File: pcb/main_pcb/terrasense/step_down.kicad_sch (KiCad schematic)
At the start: 12 parts, among them J12 12V In, U2 Mini560, U4 MPM3632CGQV-P

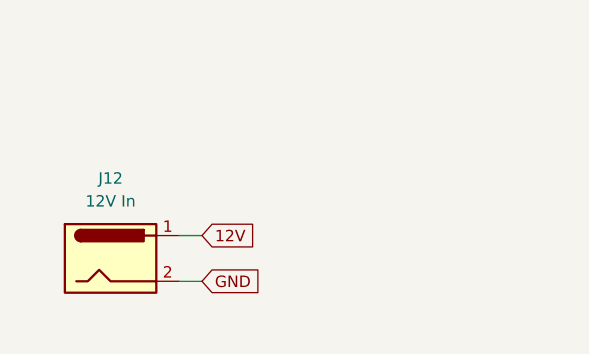
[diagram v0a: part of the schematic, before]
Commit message: update pcb with ordered pcb
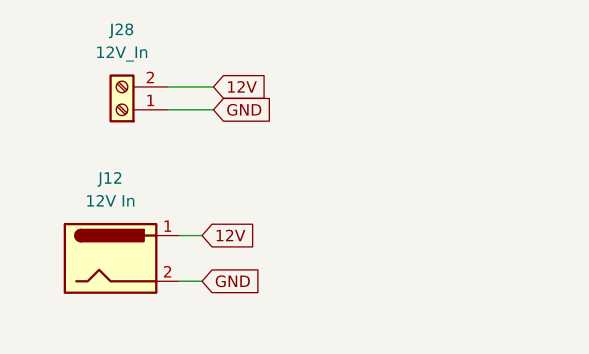
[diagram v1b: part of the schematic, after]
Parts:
- added J28: 12V_In, TerminalBlock_Altech:Altech_AK100_1x02_P5.00mm, symbol Connector:Screw_Terminal_01x02
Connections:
- net 12V: now also J28.2 (Pin_2)
- net GND: now also J28.1 (Pin_1)
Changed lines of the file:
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@@
+	(wire
+		(pts
+			(xy 46.99 25.4) (xy 52.07 25.4)
+		)
+		(stroke
+			(width 0)
+			(type default)
+		)
+	)
 	(wire
 		(pts
@@
 		(pts
 			(xy 31.75 69.85) (xy 31.75 71.12)
+		)
+		(stroke
+			(width 0)
+			(type default)
+		)
+	)
+	(wire
+		(pts
+			(xy 46.99 22.86) (xy 52.07 22.86)
 		)
 		(stroke
@@
 		)
 	)
+	(global_label "12V"
+		(shape input)
+		(at 52.07 22.86 0)
+		(effects
+			(font
+				(size 1.27 1.27)
+			)
+			(justify left)
+		)
+		(property "Intersheetrefs" "${INTERSHEET_REFS}"
+			(at 52.07 22.86 0)
+			(hide yes)
+			(show_name no)
+			(do_not_autoplace no)
+			(effects
+				(font
+					(size 1.27 1.27)
+				)
+			)
+		)
+	)
 	(global_label "GND"
 		(shape input)
@@
 		(property "Intersheetrefs" "${INTERSHEET_REFS}"
 			(at 77.47 90.17 90)
+			(hide yes)
+			(show_name no)
+			(do_not_autoplace no)
+			(effects
+				(font
+					(size 1.27 1.27)
+				)
+			)
+		)
+	)
+	(global_label "GND"
+		(shape input)
+		(at 52.07 25.4 0)
+		(effects
+			(font
+				(size 1.27 1.27)
+			)
+			(justify left)
+		)
+		(property "Intersheetrefs" "${INTERSHEET_REFS}"
+			(at 52.07 25.4 0)
 			(hide yes)
 			(show_name no)
@@
 					(unit 1)
 				)
+			)
+		)
+	)
+	(symbol
+		(lib_id "Connector:Screw_Terminal_01x02")
+		(at 41.91 25.4 180)
+		(unit 1)
+		(body_style 1)
+		(exclude_from_sim no)
+		(in_bom yes)
+		(on_board yes)
+		(in_pos_files yes)
+		(dnp no)
+		(fields_autoplaced yes)
+		(property "Reference" "J28"
+			(at 41.91 16.51 0)
+			(show_name no)
+			(do_not_autoplace no)
+			(effects
+				(font
+					(size 1.27 1.27)
+				)
+			)
+		)
+		(property "Value" "12V_In"
+			(at 41.91 19.05 0)
+			(show_name no)
+			(do_not_autoplace no)
+			(effects
+				(font
+					(size 1.27 1.27)
+				)
+			)
+		)
+		(property "Footprint" "TerminalBlock_Altech:Altech_AK100_1x02_P5.00mm"
+			(at 41.91 25.4 0)
+			(hide yes)
+			(show_name no)
+			(do_not_autoplace no)
+			(effects
+				(font
+					(size 1.27 1.27)
+				)
+			)
+		)
+		(property "Datasheet" ""
+			(at 41.91 25.4 0)
+			(hide yes)
+			(show_name no)
+			(do_not_autoplace no)
+			(effects
+				(font
+					(size 1.27 1.27)
+				)
+			)
+		)
+		(property "Description" "Generic screw terminal, single row, 01x02, script generated (kicad-library-utils/schlib/autogen/connector/)"
+			(at 41.91 25.4 0)
+			(hide yes)
+			(show_name no)
+			(do_not_autoplace no)
+			(effects
+				(font
+					(size 1.27 1.27)
+				)
+			)
+		)
+		(pin "2"
+		)
+		(pin "1"
+		)
+		(instances
+			(project "terrasense"
+				(path "/23e86ba0-86da-4b77-883c-d580cbeb388f/ac044982-d6f3-428e-96ee-435dfe5e555b"
+					(reference "J28")
+					(unit 1)
+				)
